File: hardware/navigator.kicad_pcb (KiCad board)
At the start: 4 copper layers, 65 x 56.5 mm, 45 parts, among them J1 BLDC-1, J10 GPIO, J2 BLDC-1, J3 BLDC-1, J4 BLDC-1, J5 BLDC-1, J6 BLDC-1, J7 Conn_01x02_Pin, J8 USB_C_Receptacle_USB2.0_16P, J9 Conn_01x04_Pin, SW1 SW_SPST, SW2 SW_SPST, U1 AP2112K-3.3, U2 LM2576-5.0, U3 ESP32-S3-MINI-1U, U4 INA226

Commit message: feat: update navigator hardware to revision 002
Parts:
- removed D3: D_Schottky, Diode_SMD:D_SOD-123
- removed L1: 100uH, Inductor_SMD:L_Vishay_IHLP-6767
- removed the U4 at (131.8, 75.0)
- added C11: 0.1uF, Capacitor_SMD:C_0805_2012Metric, F.Cu at (153.8, 82.7)
- added C12: 1uF, Capacitor_SMD:C_0805_2012Metric, F.Cu at (153.5, 89.8)
- added C13: 0.1uF, Capacitor_SMD:C_0805_2012Metric, F.Cu at (149.8, 58.6)
- added G***: LOGO, logo:logo, F.Cu at (142.8, 83.4)
- added R12: 2k2, Resistor_SMD:R_0805_2012Metric, F.Cu at (138.1, 59.7)
- added R13: 2k2, Resistor_SMD:R_0805_2012Metric, F.Cu at (134.6, 59.7)
- added R14: 10k, Resistor_SMD:R_0805_2012Metric, F.Cu at (159.5, 59.2)
- added R15: 10k, Resistor_SMD:R_0805_2012Metric, F.Cu at (163.1, 56.9)
- added R16: 10k, Resistor_SMD:R_0805_2012Metric, F.Cu at (163.1, 58.9)
- added R17: 10k, Resistor_SMD:R_0805_2012Metric, F.Cu at (151.3, 89.8)
- added U3: BNO086, BNO086:BNO086, F.Cu at (157.8, 55.1)
- added U5: INA226, Package_SO:TSSOP-10_3x3mm_P0.5mm, F.Cu at (148.0, 55.0)
- C1: value 0.1uF -> 100uF; footprint Capacitor_SMD:C_0805_2012Metric -> Capacitor_SMD:CP_Elec_8x10.5
- C2: value 330uF -> 10uF; footprint Capacitor_SMD:C_Elec_10x10.2 -> Capacitor_SMD:C_1210_3225Metric
- C5: value 1000uF -> 47uF; footprint Capacitor_SMD:CP_Elec_10x10.5 -> Capacitor_SMD:C_1210_3225Metric
- C7: footprint Capacitor_SMD:C_0603_1608Metric -> Capacitor_SMD:C_0805_2012Metric
- C8: value 1uF -> 0.1uF
- D1: value Schottky -> D_Schottky; footprint Diode_SMD:D_SMB -> Diode_SMD:D_SOD-123
- J7: footprint Connector_JST:JST_VH_S2P-VH_1x02_P3.96mm_Horizontal -> 282837-2:282837-2
- R11: value 10k -> 5k1
- R7: value 2k2 -> 100k; moved to F.Cu
- R8: value 2k2 -> 14k3; moved to F.Cu
- R9: value 5k1 -> 10k
- U2: value LM2576-5.0 -> MPM3550EGLE; footprint Package_TO_SOT_SMD:TO-263-5_TabPin3 -> Package_LGA:MPS_LGA-18-10EP_12x12mm_P3.3mm
- moved R11 46.5 mm to (109.9, 59.0), turned to 180 degrees
- moved R9 45.3 mm to (154.9, 61.0), turned to 90 degrees
- moved C4 44.9 mm to (129.3, 83.4), turned to -90 degrees
- moved U1 43.8 mm to (126.1, 83.3)
- moved C3 43.7 mm to (122.9, 83.3), turned to 90 degrees
- moved J6 42.9 mm to (113.4, 95.6)
- moved J1 42.9 mm to (156.7, 95.6)
- moved R6 42.7 mm to (110.9, 92.4)
- moved R1 42.6 mm to (153.9, 92.4)
- moved R7 40.8 mm to (118.7, 76.3), turned to 90 degrees
- moved R8 40.6 mm to (118.7, 69.8), turned to -90 degrees
- moved D2 36.5 mm to (116.6, 61.4)
- moved J9 32.9 mm to (136.3, 54.9)
- moved C9 28.8 mm to (157.5, 59.2), turned to -90 degrees
- moved C5 28.6 mm to (103.4, 69.7), turned to -90 degrees
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- renumbered U3 to U4
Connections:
- C1 pad 1: GND -> +BATT
- C1 pad 2: +BATT -> GND
- C10 pad 1: /BOOT -> +3V3
- C2 pad 1: +BATT -> GND
- C2 pad 2: GND -> +BATT
- C8 pad 1: /RST -> +3V3
- C9 pad 1: +3V3 -> Net-(U3-CAP)
- D1 pad 1: Net-(D1-K) -> +5V
- D1 pad 2: GND -> /USB_5V
- D2 pad 2: /USB_5V -> /BUCK_5V
- J1 pad 3: Net-(J1-Pin_3) -> GND
- R1 pad 2: Net-(J1-Pin_3) -> GND
- R10 pad 1: GND -> Net-(J8-CC1)
- R10 pad 2: Net-(J8-CC2) -> GND
- R11 pad 1: +3V3 -> GND
- R11 pad 2: /RST -> Net-(J8-CC2)
- R7 pad 1: +3V3 -> GND
- R7 pad 2: /I2C_SCL -> Net-(U2-RFREQ)
- R8 pad 1: +3V3 -> Net-(U2-FB)
- R8 pad 2: /I2C_SDA -> GND
- R9 pad 1: Net-(J8-CC1) -> +3V3
- R9 pad 2: GND -> Net-(U3-~{BOOT})
- SW1 pad 2: /RST -> /BOOT
- SW2 pad 2: /BOOT -> /RST
- U2 pad 1: +BATT -> unconnected-(U2-EN-Pad1)
- U2 pad 2: Net-(D1-K) -> Net-(U2-RFREQ)
- U2 pad 3: GND -> unconnected-(U2-PGOOD-Pad3)
- U2 pad 4: /BUCK_5V -> Net-(U2-FB)
- U2 pad 5: GND -> /BUCK_5V
- U4 pad 21: unconnected-(U3-IO17-Pad21) -> /GPIO15/RXD0
- U4 pad 22: unconnected-(U3-IO18-Pad22) -> /GPIO14/TXD0
- U4 pad 39: /GPIO15/RXD0 -> unconnected-(U4-TXD0-Pad39)
- U4 pad 40: /GPIO14/TXD0 -> unconnected-(U4-RXD0-Pad40)
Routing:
- net +BATT: track 39.2 -> 80.8 mm, vias 0 -> 1
- net /BLDC_6: track 4.37 -> 42.7 mm, vias 0 -> 1
- net Net-(D1-K): track 37.7 -> 0.00 mm
- net /BLDC_5: track 4.35 -> 38.8 mm, vias 0 -> 1
- net /BLDC_1: track 4.26 -> 35.8 mm, vias 0 -> 1
- net /BLDC_4: track 4.32 -> 35.0 mm, vias 0 -> 1
- net /BLDC_2: track 4.28 -> 33.1 mm, vias 0 -> 1
- net /USB_5V: track 46.5 -> 19.6 mm
- net /BLDC_3: track 4.30 -> 31.1 mm, vias 0 -> 1
- net /USB_D-: track 3.67 -> 29.8 mm, vias 1 -> 2
- net /USB_D+: track 1.91 -> 26.0 mm, vias 1 -> 2
- net /RST: track 21.0 -> 41.3 mm
- net +5V: track 14.9 -> 34.9 mm
- net /GPIO14/TXD0: track 45.0 -> 25.0 mm, vias 1 -> 0
- net /GPIO15/RXD0: track 41.4 -> 23.6 mm, vias 1 -> 0
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- removed copper zone on In2.Cu, net /BUCK_5V
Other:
- board text added: "01 --> BLDC_1 02 --> BLDC_2 03 --> BLDC_3 04 --> BLDC_4 05 --> BLDC_5 06 --> BLDC_6 07 --> I2C_SCL 08 <-> I2C_SDA 17 --> UART_TX 18 <-- UART_RX"
- board text added: "Designed by alexs (getriscvyy)"
- board text added: "NAVIGATOR"
- board text added: "{ "ViaStitcher": "0.3.1", "stitch_zone_0": { "HSpacing": "1", "VSpacing": "1", "HOffset": "0", "VOffset": "0", "Clearance": "0", "Randomize": false, "Stagger": true, "OnlyFilledCopper": true }, "stitch_zone_1": { "HSpacing": "5", "VSpacing": "5", "HOffset": "0", "VOffset": "0", "Clearance": "0.5", "Randomize": false, "Stagger": false, "OnlyFilledCopper": true } }"
- board text removed: "BLDC_1"
- board text removed: "BLDC_2"
- board text removed: "BLDC_3"
- board text removed: "BLDC_4"
- board text removed: "BLDC_5"
- board text removed: "BLDC_6"

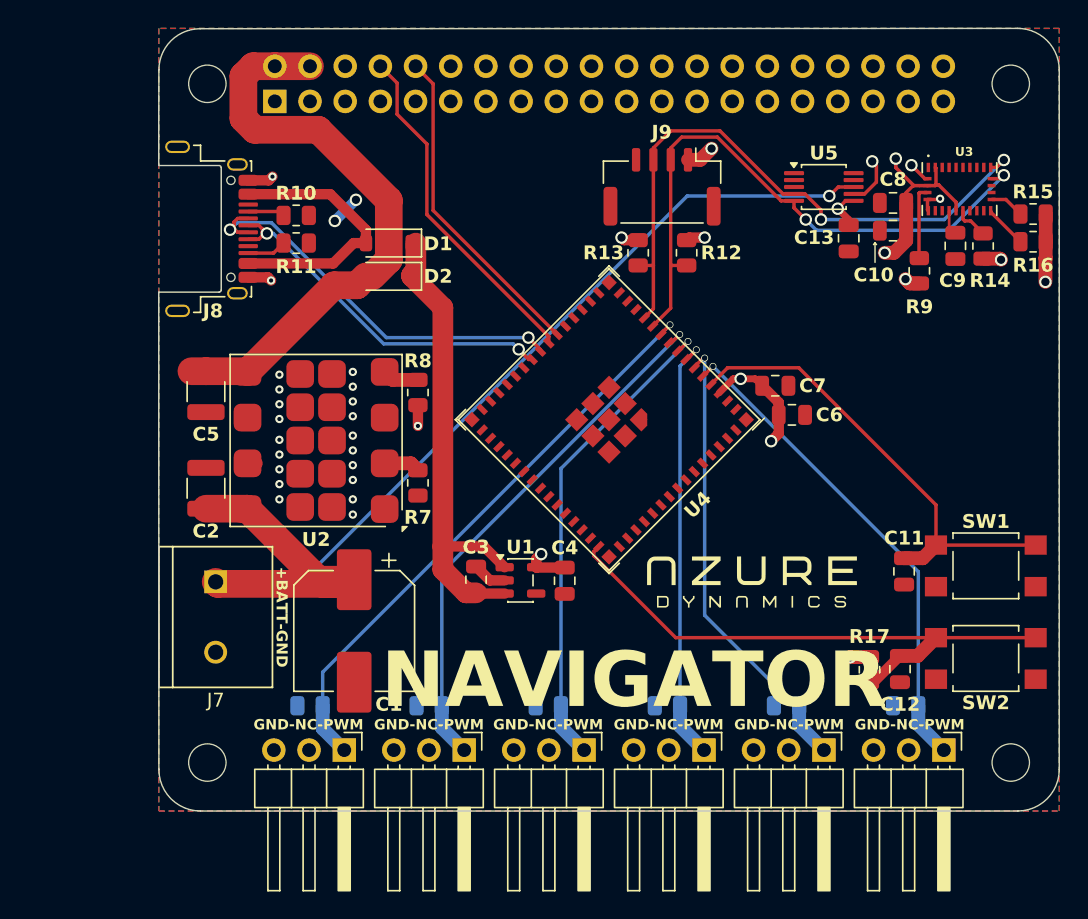
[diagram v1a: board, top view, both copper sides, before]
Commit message: fix: clean up pcb silkscreen and designators
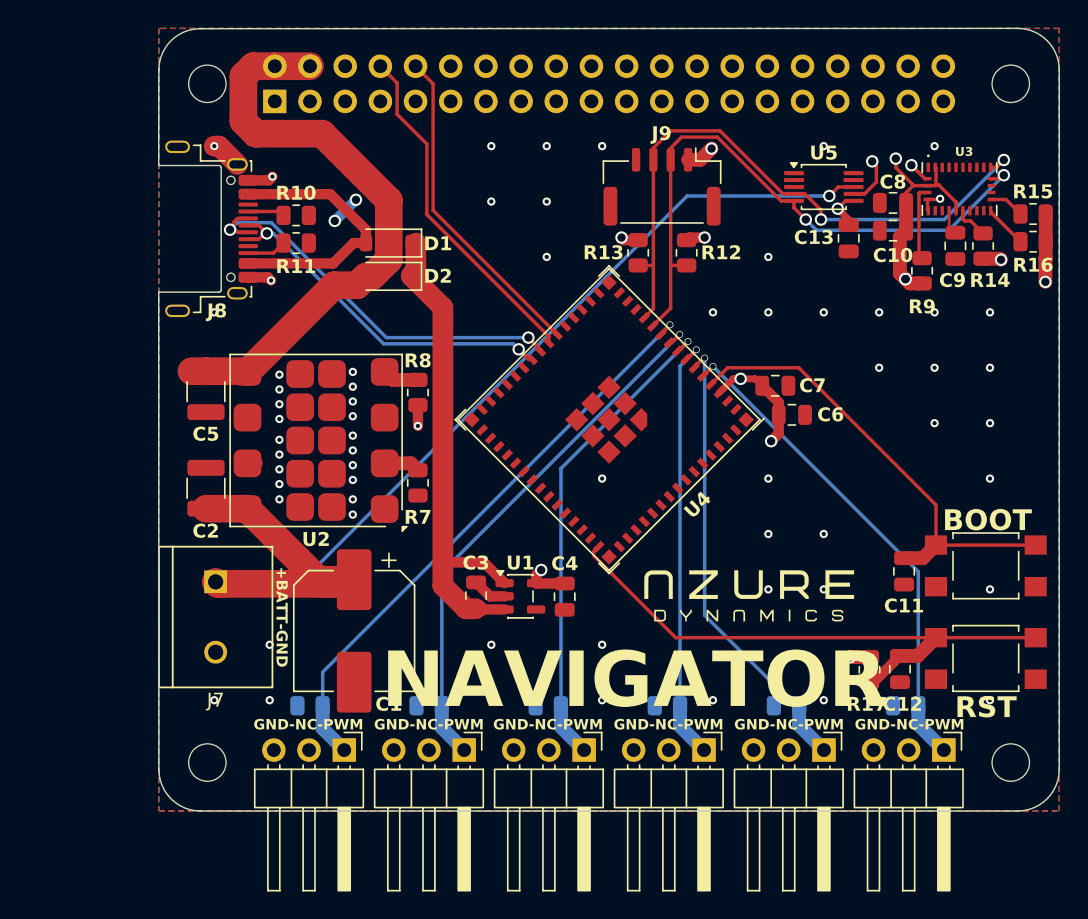
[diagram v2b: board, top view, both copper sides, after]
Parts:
- moved C3 1.15 mm to (122.9, 84.5)
- moved C4 1.15 mm to (129.3, 84.5)
- moved U1 1.15 mm to (126.1, 84.5)
- moved G*** 1.02 mm to (142.6, 84.4)
- moved R9 0.20 mm to (155.1, 61.0)
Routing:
- net GND: track 17.3 -> 19.5 mm, vias 27 -> 67
- net +3V3: track 42.4 -> 43.8 mm
- net +5V: track 34.9 -> 36.0 mm
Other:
- board text added: "BOOT"
- board text added: "RST"
- board text added: "{ "ViaStitcher": "0.3.1", "stitch_zone_0": { "HSpacing": "1", "VSpacing": "1", "HOffset": "0", "VOffset": "0", "Clearance": "0", "Randomize": false, "Stagger": true, "OnlyFilledCopper": true }, "stitch_zone_1": { "HSpacing": "4", "VSpacing": "4", "HOffset": "0", "VOffset": "0", "Clearance": "0.5", "Randomize": false, "Stagger": false, "OnlyFilledCopper": true } }"
- board text removed: "{ "ViaStitcher": "0.3.1", "stitch_zone_0": { "HSpacing": "1", "VSpacing": "1", "HOffset": "0", "VOffset": "0", "Clearance": "0", "Randomize": false, "Stagger": true, "OnlyFilledCopper": true }, "stitch_zone_1": { "HSpacing": "5", "VSpacing": "5", "HOffset": "0", "VOffset": "0", "Clearance": "0.5", "Randomize": false, "Stagger": false, "OnlyFilledCopper": true } }"
